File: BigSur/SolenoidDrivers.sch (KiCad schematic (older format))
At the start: 32 parts, among them U1 DRV103H, U2 DRV103H, U3 DRV8806

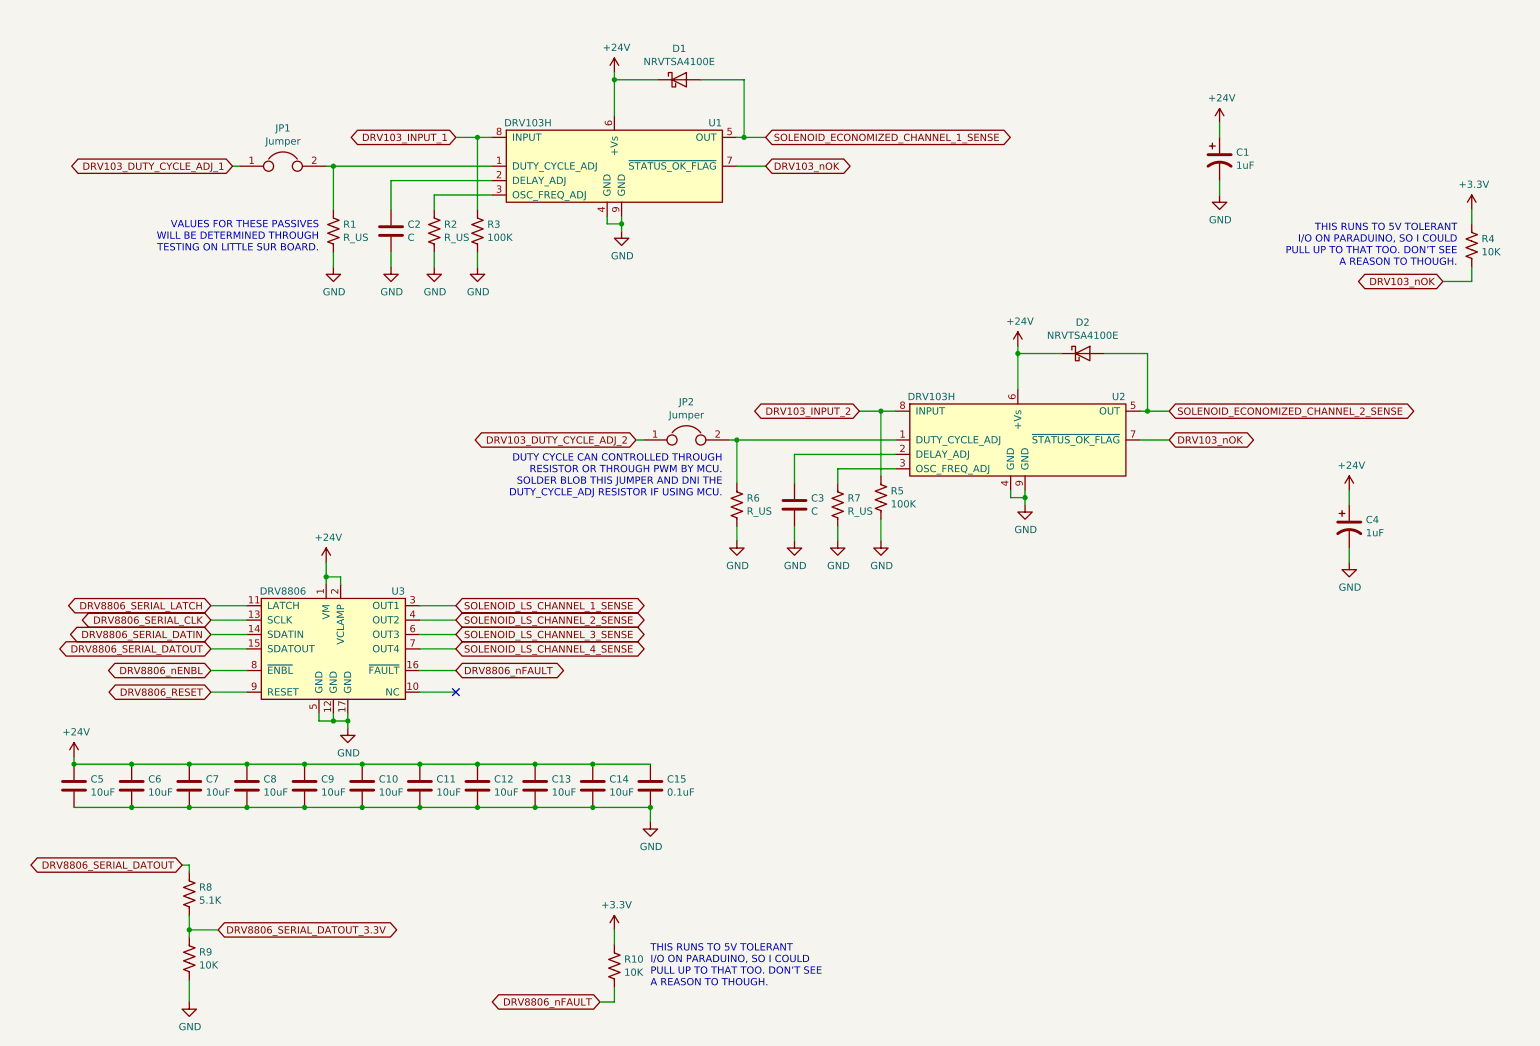
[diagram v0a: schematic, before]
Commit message: Added mounting holes, CAN connector,  indicator LEDs, started general purpose relays
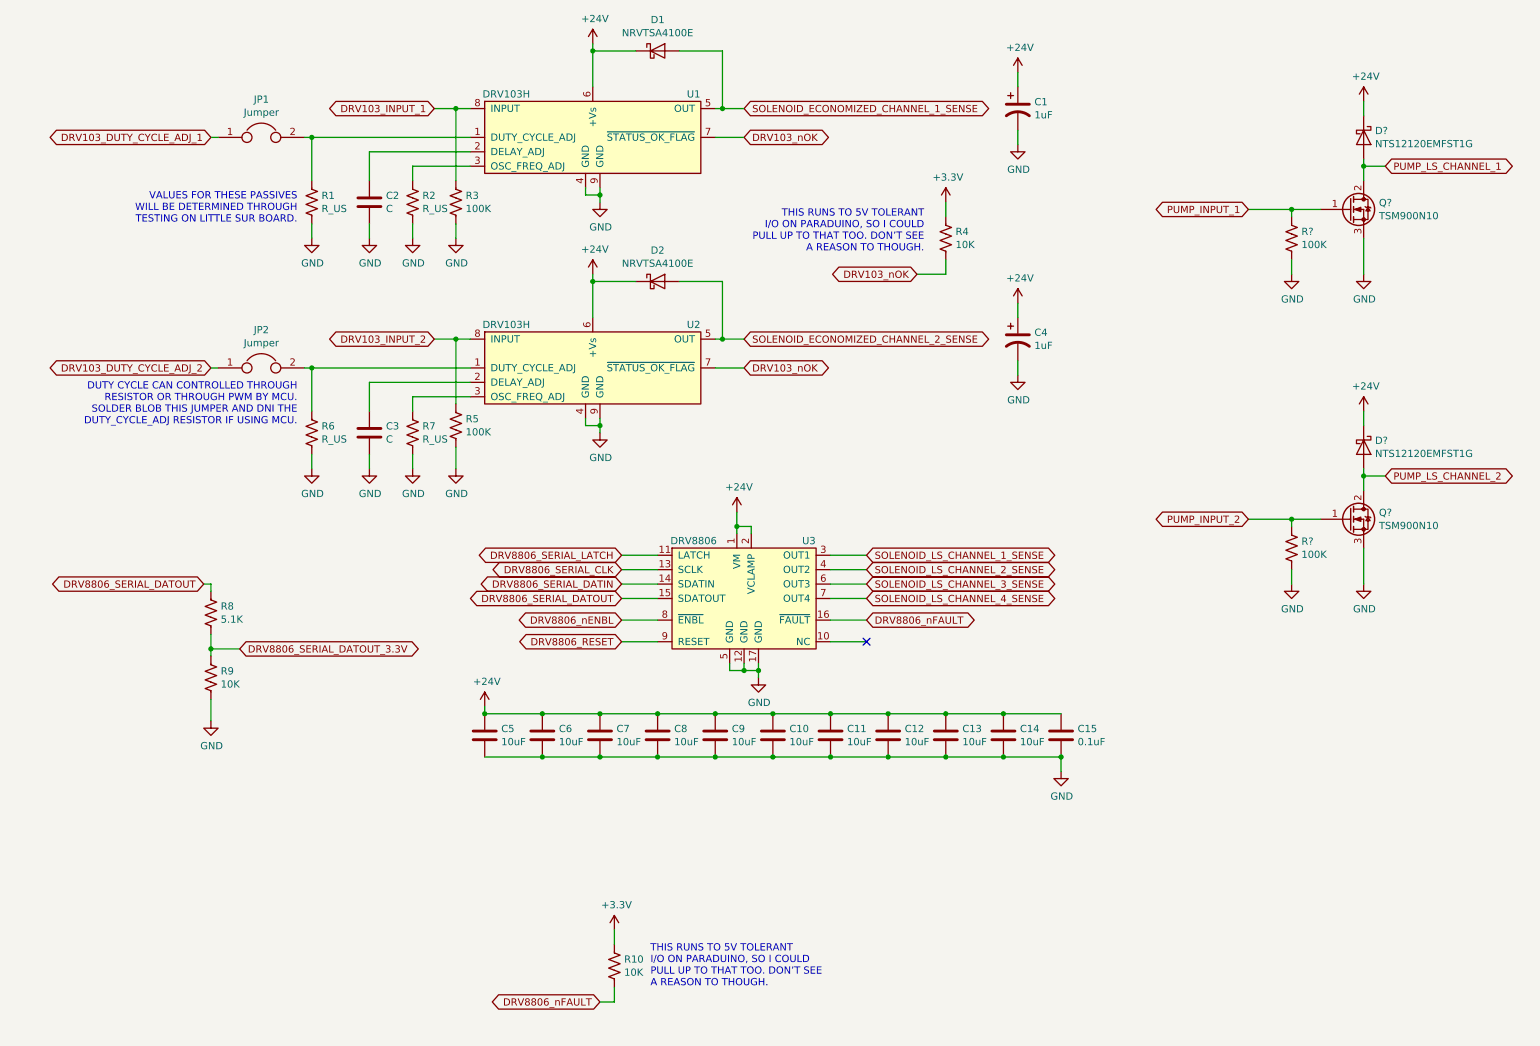
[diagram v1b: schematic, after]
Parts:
- added D? (x2): NTS12120EMFST1G, BigSur:ONSemi_SMD_Schottky_NTS12120EMFS, symbol Device:D_Schottky
- added Q? (x2): TSM900N10, Package_TO_SOT_SMD:TO-252-2, symbol Device:Q_NMOS_GDS
- added R? (x2): 100K, Resistor_SMD:R_0603_1608Metric_Pad1.05x0.95mm_HandSolder, symbol Device:R_US
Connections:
- net +24V: now also D?.1 (K), D?.1 (K)
- net GND: now also Q?.3 (S), Q?.3 (S), R?.2, R?.2
- new net PUMP_INPUT_1: Q?.1 (G), R?.1
- new net PUMP_INPUT_2: Q?.1 (G), R?.1
- new net PUMP_LS_CHANNEL_1: D?.2 (A), Q?.2 (D)
- new net PUMP_LS_CHANNEL_2: D?.2 (A), Q?.2 (D)
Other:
- moved on the sheet: C1, C10, C11, C12, C13, C14, C15, C2, C3, C4, C5, C6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
